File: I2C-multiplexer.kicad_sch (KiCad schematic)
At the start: 3 parts, among them U601 PCA9548ARGE

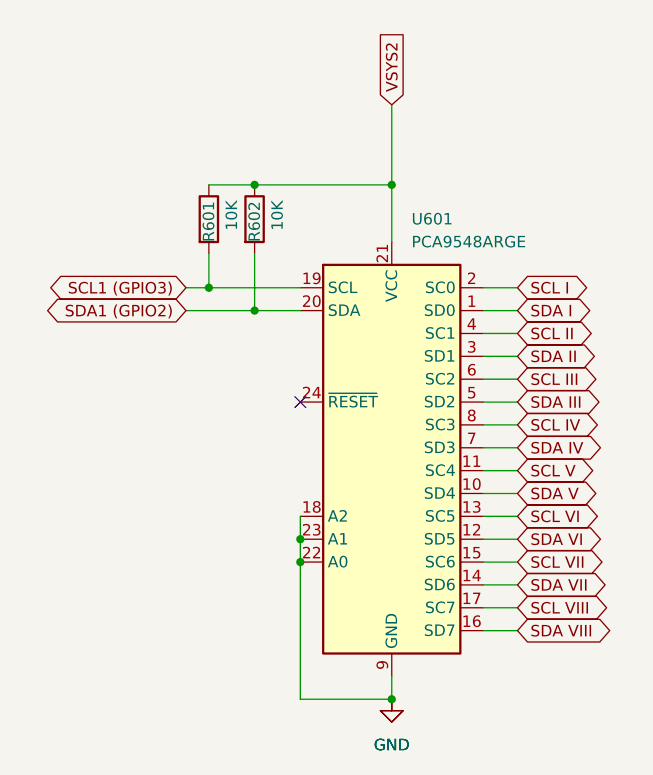
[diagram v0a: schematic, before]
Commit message: CM4>RP3/4
changed SBC to RP3/4
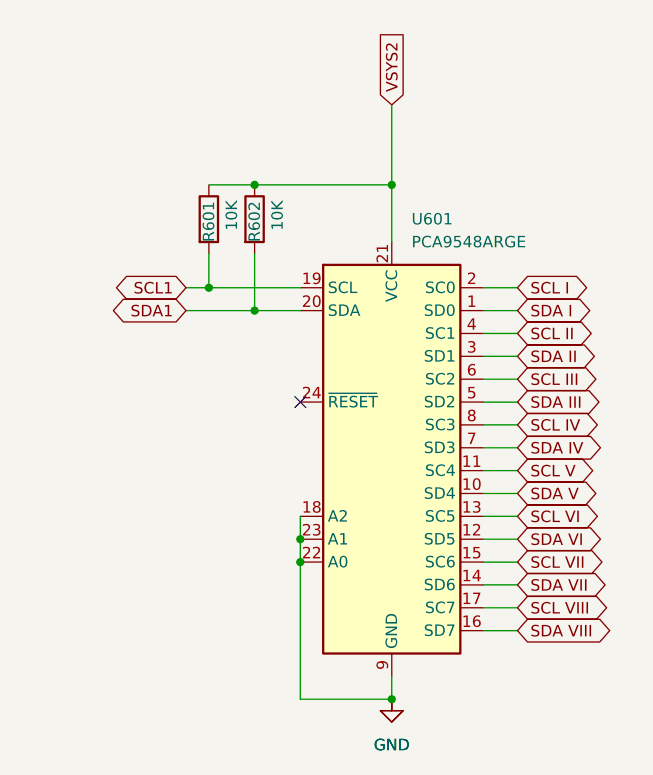
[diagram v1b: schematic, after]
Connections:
- net SCL1 (GPIO3) renamed SCL1
- net SDA1 (GPIO2) renamed SDA1
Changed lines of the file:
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@@
-		)
-	)
-	(global_label "SCL1 (GPIO3)"
-		(shape bidirectional)
-		(at 35.56 46.99 180)
-		(effects
-			(font
-				(size 1.27 1.27)
-				(color 64 145 0 1)
-			)
-			(justify right)
-		)
-		(property "Intersheetrefs" "${INTERSHEET_REFS}"
-			(at 35.56 46.99 0)
-			(effects
-				(font
-					(size 1.27 1.27)
-				)
-				(hide yes)
-			)
 		)
 	)
@@
 				)
 				(justify left)
-				(hide yes)
-			)
-		)
-	)
-	(global_label "SDA1 (GPIO2)"
-		(shape bidirectional)
-		(at 35.56 49.53 180)
-		(effects
-			(font
-				(size 1.27 1.27)
-				(color 64 145 0 1)
-			)
-			(justify right)
-		)
-		(property "Intersheetrefs" "${INTERSHEET_REFS}"
-			(at 35.56 49.53 0)
-			(effects
-				(font
-					(size 1.27 1.27)
-				)
 				(hide yes)
 			)
@@
 				(hide yes)
 			)
+		)
+	)
+	(global_label "SCL1"
+		(shape bidirectional)
+		(at 35.56 46.99 180)
+		(effects
+			(font
+				(size 1.27 1.27)
+				(color 64 145 0 1)
+			)
+			(justify right)
+		)
+		(property "Intersheetrefs" "${INTERSHEET_REFS}"
+			(at 35.56 46.99 0)
+			(effects
+				(font
+					(size 1.27 1.27)
+				)
+				(hide yes)
+			)
+		)
+	)
+	(global_label "SDA1"
+		(shape bidirectional)
+		(at 35.56 49.53 180)
+		(effects
+			(font
+				(size 1.27 1.27)
+				(color 64 145 0 1)
+			)
+			(justify right)
+		)
+		(property "Intersheetrefs" "${INTERSHEET_REFS}"
+			(at 35.56 49.53 0)
+			(effects
+				(font
+					(size 1.27 1.27)
+				)
+				(hide yes)
+			)
